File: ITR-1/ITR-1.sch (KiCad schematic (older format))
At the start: 50 parts, among them K1 Кнопка_KLS7-TS5401-1.35-250-T, K2 Кнопка_KLS7-TS5401-1.35-250-T, X1 отверстие_под_пайку, X2 отверстие_под_пайку

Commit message: аналоговые каналы перенесены на ADC1
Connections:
- net AN.2V5.REF: now also A1.8 (IO32/ADC1-4); no longer A1.12 (IO27/ADC2-7)
- net AN.BAT.MEASURE: now also A1.7 (IO35/ADC1-7); no longer A1.26 (IO4/ADC2-0)
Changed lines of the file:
@@
 Wire Wire Line
 	11000 3500 11675 3500
-Text Label 6750 10300 2    50   ~ 0
+Text Label 1750 9400 0    50   ~ 0
 AN.BAT.MEASURE
-Text Label 2000 10150 0    50   ~ 0
+Text Label 1750 9550 0    50   ~ 0
 AN.2V5.REF
 NoConn ~ 4650 10750
 NoConn ~ 2500 10300
 Wire Wire Line
-	6750 10300 5950 10300
+	1750 9400 2500 9400
 Wire Wire Line
 	5950 10000 6750 10000
@@
 $EndComp
 Wire Wire Line
-	2500 10150 2000 10150
+	2500 9550 1750 9550
 NoConn ~ 4800 10750
 $Comp

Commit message: изменено опорное + подключение к мотору; заготовка под 2 светодиода
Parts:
- added HL2: Светодиод_сдвоенный_KPB-3025SURKCGKC, N_VD_HL:Светодиод_SMD_m3025, symbol elements_2020:Светодиод_сдвоенный_KPB-3025SURKCGKC
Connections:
- net U.FB: now reaches DA1.1, R14.2, R15.1
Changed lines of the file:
@@
 Wire Wire Line
 	13000 1750 13000 4750
+Text Label 14500 5600 0    50   ~ 0
+U.FB
+$Comp
+L elements_2020:Светодиод_сдвоенный_KPB-3025SURKCGKC HL2
+U 1 1 6172B487
+P 8500 8800
+F 0 "HL2" H 8650 9031 60  0000 C CNN
+F 1 "Светодиод_сдвоенный_KPB-3025SURKCGKC" H 8650 9031 60  0001 C CNN
+F 2 "N_VD_HL:Светодиод_SMD_m3025" H 8800 8300 60  0001 C CNN
+F 3 "" H 8800 8300 60  0001 C CNN
+	1    8500 8800
+	1    0    0    -1
+$EndComp
 $EndSCHEMATC

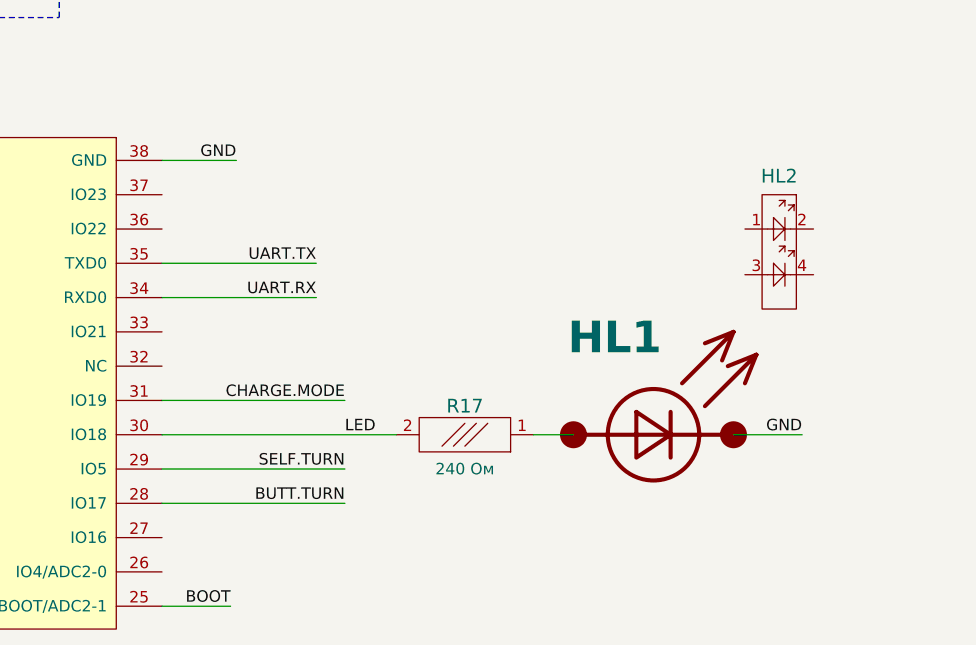
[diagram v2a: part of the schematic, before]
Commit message: модифицирована тайминги обмена с сервером, LED заменен на 2хцветный
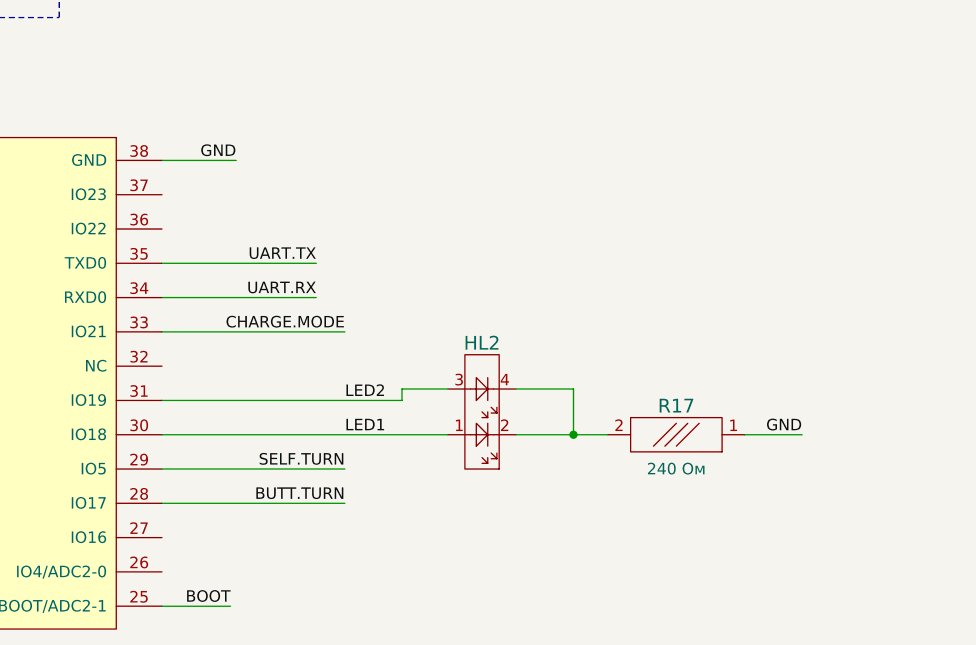
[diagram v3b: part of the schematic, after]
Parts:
- removed HL1: Светодиод, N_VD_HL:Светодиод_SMD_IEC_0603, symbol ITR-1-rescue:Светодиод-BIG_schemes
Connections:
- net CHARGE.MODE: now also A1.33 (IO21); no longer A1.31 (IO19)
- net GND: now also R17.1
- net LED1: now reaches HL2.1
- net LED1: now also A1.30 (IO18)
- net at HL2.2: now also HL2.4, R17.2
- net LED2: now reaches HL2.3
- net LED2: now also A1.31 (IO19)
- removed net LED: A1.30 (IO18), R17.2
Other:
- moved on the sheet: HL2, R17
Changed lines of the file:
@@
 Text Label 6275 8500 2    50   ~ 0
 GND
-Text Label 6750 9550 2    50   ~ 0
+Text Label 6750 9250 2    50   ~ 0
 CHARGE.MODE
 Text Label 6750 10000 2    50   ~ 0
@@
 	6625 8950 5950 8950
 Wire Wire Line
-	6750 9550 5950 9550
+	6750 9250 5950 9250
 Text Label 6250 10450 2    50   ~ 0
 BOOT
@@
 NoConn ~ 3600 10750
 Text Label 6750 9700 0    50   ~ 0
-LED
+LED1
 $Comp
 L elements:Клеммник_х3 XS2
@@
 L elements:Резистор_0,065Вт R17
 U 1 1 61468C4F
-P 7275 9700
-F 0 "R17" H 7275 9575 60  0000 C CNN
-F 1 "Резистор_0,065Вт" H 7275 9550 60  0001 C CNN
-F 2 "N_RLC:Резистор_SMD_0603_0,065_Вт" H 7275 9700 60  0001 C CNN
-F 3 "" H 7275 9700 60  0001 C CNN
-F 4 "R101" H 7275 9700 50  0001 C CNN "УГО"
-F 5 "240 Ом" H 7275 9850 50  0000 C CNN "INFO"
-	1    7275 9700
+P 8200 9700
+F 0 "R17" H 8200 9575 60  0000 C CNN
+F 1 "Резистор_0,065Вт" H 8200 9550 60  0001 C CNN
+F 2 "N_RLC:Резистор_SMD_0603_0,065_Вт" H 8200 9700 60  0001 C CNN
+F 3 "" H 8200 9700 60  0001 C CNN
+F 4 "R101" H 8200 9700 50  0001 C CNN "УГО"
+F 5 "240 Ом" H 8200 9850 50  0000 C CNN "INFO"
+	1    8200 9700
 	-1   0    0    1
 $EndComp
@@
 Wire Wire Line
 	5950 10000 6750 10000
-$Comp
-L ITR-1-rescue:Светодиод-BIG_schemes HL1
-U 1 1 61662DE6
-P 7750 9700
-F 0 "HL1" H 7725 10125 138 0000 L CNB
-F 1 "Светодиод" H 7850 9900 50  0001 C CNN
-F 2 "N_VD_HL:Светодиод_SMD_IEC_0603" H 8025 9700 50  0001 C CNN
-F 3 "" H 8025 9700 50  0001 C CNN
-F 4 "2.730" H 7850 10000 50  0001 C CNN "SYMBOL"
-	1    7750 9700
-	1    0    0    -1
-$EndComp
-Wire Wire Line
-	7575 9700 7750 9700
-Wire Wire Line
-	8450 9700 8750 9700
 Text Label 8750 9700 2    50   ~ 0
 GND
-Wire Wire Line
-	5950 9700 6975 9700
 Wire Wire Line
 	5950 9850 6750 9850
@@
 L elements_2020:Светодиод_сдвоенный_KPB-3025SURKCGKC HL2
 U 1 1 6172B487
-P 8500 8800
-F 0 "HL2" H 8650 9031 60  0000 C CNN
-F 1 "Светодиод_сдвоенный_KPB-3025SURKCGKC" H 8650 9031 60  0001 C CNN
-F 2 "N_VD_HL:Светодиод_SMD_m3025" H 8800 8300 60  0001 C CNN
-F 3 "" H 8800 8300 60  0001 C CNN
-	1    8500 8800
-	1    0    0    -1
-$EndComp
+P 7200 9700
+F 0 "HL2" H 7350 9300 60  0000 C CNN
+F 1 "Светодиод_сдвоенный_KPB-3025SURKCGKC" H 7350 9931 60  0001 C CNN
+F 2 "N_VD_HL:Светодиод_SMD_m3025" H 7500 9200 60  0001 C CNN
+F 3 "" H 7500 9200 60  0001 C CNN
+	1    7200 9700
+	1    0    0    1
+$EndComp
+Text Label 6750 9550 0    50   ~ 0
+LED2
+Wire Wire Line
+	5950 9700 7200 9700
+Wire Wire Line
+	5950 9550 7000 9550
+Wire Wire Line
+	7000 9550 7000 9500
+Wire Wire Line
+	7000 9500 7200 9500
+Wire Wire Line
+	7500 9700 7750 9700
+Wire Wire Line
+	7750 9500 7750 9700
+Wire Wire Line
+	7750 9500 7500 9500
+Wire Wire Line
+	7900 9700 7750 9700
+Connection ~ 7750 9700
+Wire Wire Line
+	8750 9700 8500 9700
 $EndSCHEMATC

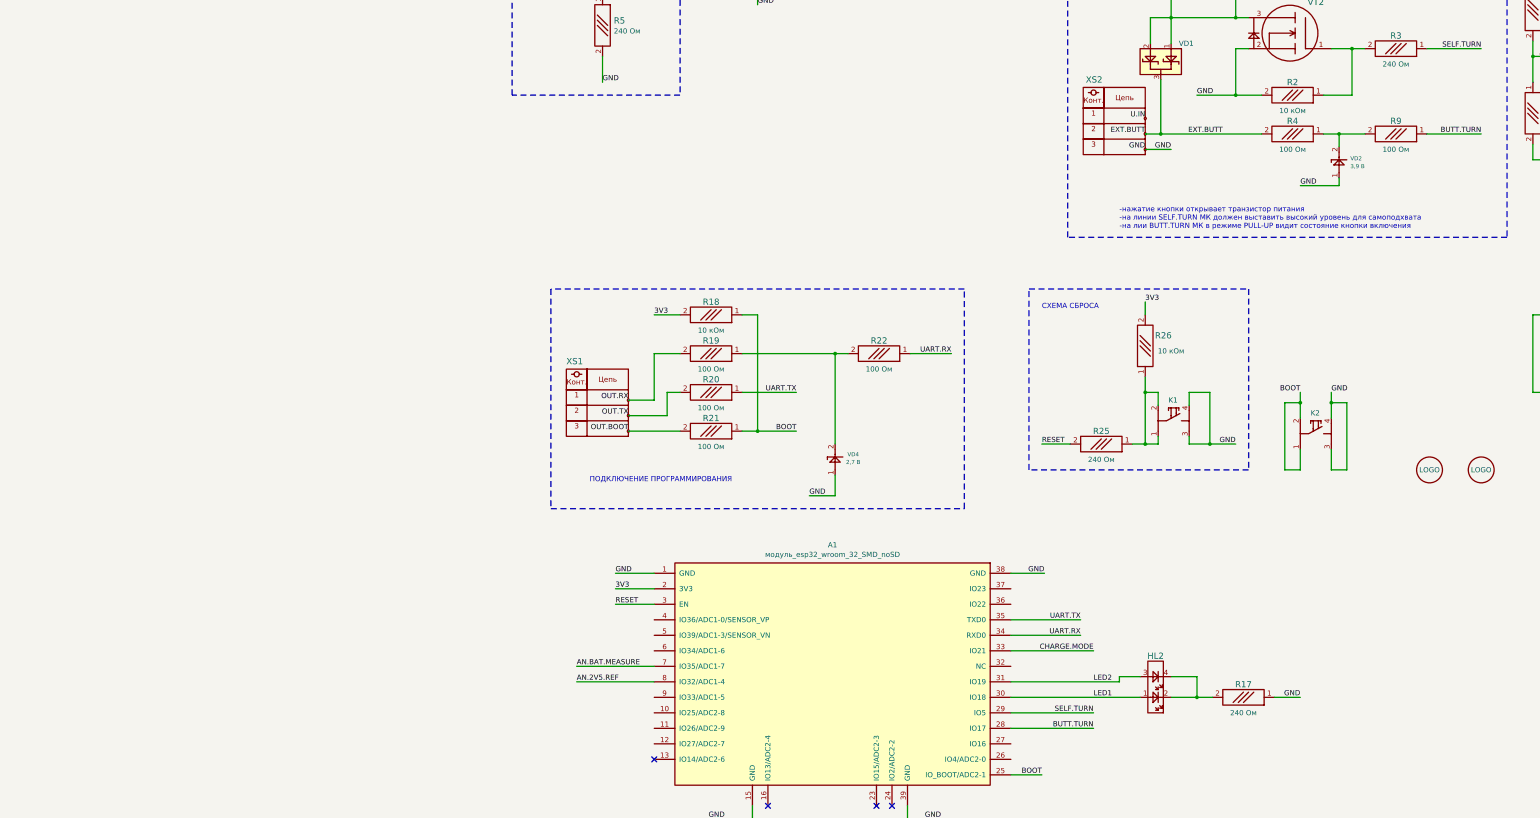
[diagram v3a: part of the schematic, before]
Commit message: зарядка через USB, в сервисный джек добавлена земля, кнопка впаивается
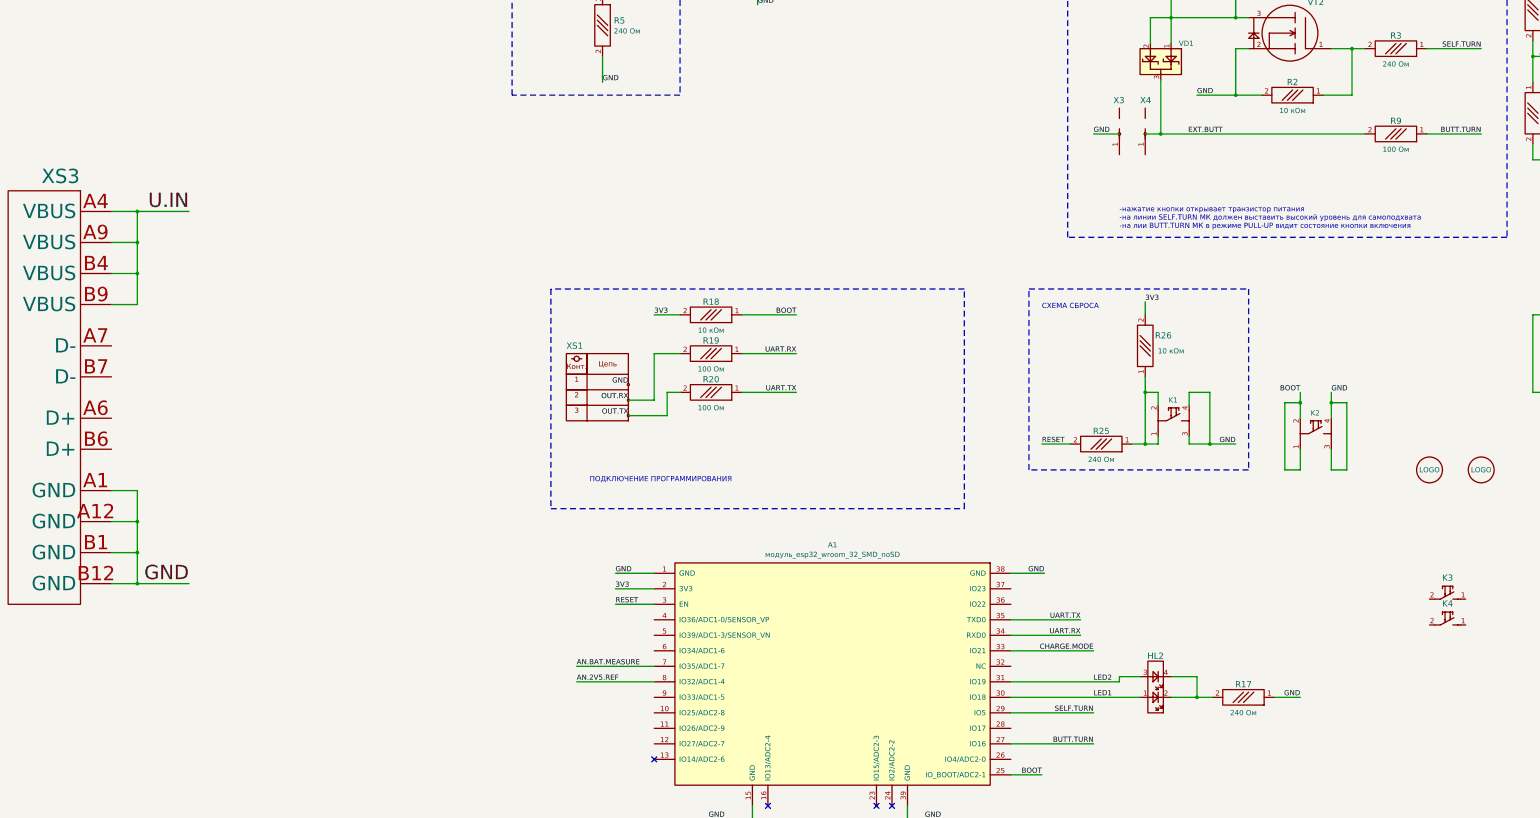
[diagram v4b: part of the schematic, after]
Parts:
- removed R21, R22, R4: Резистор_0,065Вт, N_RLC:Резистор_SMD_0603_0,065_Вт, symbol elements:Резистор_0,065Вт
- removed VD2: Стабилитрон_BZV55-C3V9, N_VD_HL:SOD-80, symbol elements_2020:Стабилитрон_1N5352BRLG_вертикальный
- removed VD4: Стабилитрон_BZV55C2V7, N_VD_HL:SOD-80, symbol elements_2020:Стабилитрон_1N5352BRLG_вертикальный
- removed XS2: Клеммник_х3, N_X:jack_ST-033, symbol elements:Клеммник_х3
- added K3, K4: кнопка, N_X:Кнопка_FSMSM, symbol elements:кнопка
- added X3, X4: отверстие_под_пайку, N_X:ОтверстиеD1.2, symbol elements:отверстие_под_пайку
- added XS3: UBS-type-C-105450-0101&упрощенная, N_X:usb-type-c, symbol elements_2020:UBS-type-C-105450-0101&упрощенная
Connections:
- net OUT.BOOT is gone; now on net OUT.TX: XS1.3
- net BUTT.TURN: now also A1.27 (IO16); no longer A1.28 (IO17)
- net EXT.BUTT: now also R9.2, X4.1
- net GND: now also XS1.1, X3.1, XS3.A1 (GND), XS3.A12 (GND), XS3.B1 (GND), XS3.B12 (GND)
- net OUT.RX: now also XS1.2; no longer XS1.1
- net OUT.TX: no longer XS1.2
- net U.IN: now also XS3.A4 (VBUS), XS3.A9 (VBUS), XS3.B4 (VBUS), XS3.B9 (VBUS)
- net UART.RX: now also R19.1
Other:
- moved on the sheet: XS1
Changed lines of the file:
@@
 EESchema Schematic File Version 4
-LIBS:ITR-1-cache
 EELAYER 30 0
 EELAYER END
@@
 ~~300 мА
 Wire Wire Line
-	7250 4400 7500 4400
+	7000 4250 6750 4250
 Wire Wire Line
 	8125 3875 7750 3875
@@
 Text Label 7750 3875 0    50   ~ 0
 GND
-Text Label 7500 4400 2    50   ~ 0
+Text Label 6750 4250 0    50   ~ 0
 GND
 Connection ~ 8125 3125
@@
 Wire Wire Line
 	10500 4250 9975 4250
-Wire Wire Line
-	9375 4250 9125 4250
 Connection ~ 7400 4250
 Text Notes 7000 5175 0    50   ~ 0
@@
 Text Label 6750 9250 2    50   ~ 0
 CHARGE.MODE
-Text Label 6750 10000 2    50   ~ 0
+Text Label 6750 10150 2    50   ~ 0
 BUTT.TURN
 Text Label 2125 8800 0    50   ~ 0
@@
 Text Label 6750 9700 0    50   ~ 0
 LED1
-$Comp
-L elements:Клеммник_х3 XS2
-U 1 1 6149F023
-P 7250 4100
-F 0 "XS2" H 6675 4475 60  0000 L CNN
-F 1 "Клеммник_х3" H 6950 3700 60  0001 C CNN
-F 2 "N_X:jack_ST-033" H 6675 4375 60  0001 C CNN
-F 3 "" H 6675 4375 60  0001 C CNN
-F 4 "https://www.chipdip.ru/product/st-033" H 7250 4100 50  0001 C CNN "LINK"
-	1    7250 4100
-	1    0    0    -1
-$EndComp
-Text Label 7250 4400 2    50   ~ 0
+Text Label -2000 8600 2    138  ~ 0
 GND
-Text Label 7250 4100 2    50   ~ 0
+Text Label -2000 5000 2    138  ~ 0
 U.IN
 Text Label 8000 4250 2    50   ~ 0
 EXT.BUTT
-Text Label 7250 4250 2    50   ~ 0
-EXT.BUTT
 Text Label 2250 6975 2    50   ~ 0
 OUT.TX
@@
 Wire Wire Line
 	2500 6375 2750 6375
-Text Label 4000 7750 0    50   ~ 0
-GND
-$Comp
-L elements:Резистор_0,065Вт R22
-U 1 1 61539EA6
-P 4675 6375
-F 0 "R22" H 4675 6250 60  0000 C CNN
-F 1 "Резистор_0,065Вт" H 4675 6225 60  0001 C CNN
-F 2 "N_RLC:Резистор_SMD_0603_0,065_Вт" H 4675 6375 60  0001 C CNN
-F 3 "" H 4675 6375 60  0001 C CNN
-F 4 "R101" H 4675 6375 50  0001 C CNN "УГО"
-F 5 "100 Ом" H 4675 6525 50  0000 C CNN "INFO"
-	1    4675 6375
-	-1   0    0    1
-$EndComp
-Text Label 5375 6375 2    50   ~ 0
+Text Label 3875 6375 2    50   ~ 0
 UART.RX
 Text Label 3875 6750 2    50   ~ 0
 UART.TX
 Wire Wire Line
-	4975 6375 5375 6375
+	3350 6375 3875 6375
 Text Notes 1875 7625 0    50   ~ 0
 ПОДКЛЮЧЕНИЕ ПРОГРАММИРОВАНИЯ
-Text Label 3875 7125 2    50   ~ 0
+Text Label 3875 6000 2    50   ~ 0
 BOOT
-$Comp
-L elements:Резистор_0,065Вт R21
-U 1 1 615C937D
-P 3050 7125
-F 0 "R21" H 3050 7000 60  0000 C CNN
-F 1 "Резистор_0,065Вт" H 3050 6975 60  0001 C CNN
-F 2 "N_RLC:Резистор_SMD_0603_0,065_Вт" H 3050 7125 60  0001 C CNN
-F 3 "" H 3050 7125 60  0001 C CNN
-F 4 "R101" H 3050 7125 50  0001 C CNN "УГО"
-F 5 "100 Ом" H 3050 7275 50  0000 C CNN "INFO"
-	1    3050 7125
-	-1   0    0    1
-$EndComp
-$Comp
-L elements_2020:Стабилитрон_1N5352BRLG_вертикальный VD4
-U 1 1 615D0D90
-P 4250 7550
-F 0 "VD4" V 4450 7375 39  0000 C CNN
-F 1 "Стабилитрон_BZV55C2V7" H 4425 7325 39  0001 C CNN
-F 2 "N_VD_HL:SOD-80" H 4400 7225 39  0001 C CNN
-F 3 "" H 4150 7550 39  0001 C CNN
-F 4 "2,7 В" V 4375 7375 39  0000 C CNN "INFO"
-F 5 "https://www.chipdip.ru/product/bzv55c2v7" H 4400 7125 50  0001 C CNN "LINK"
-	1    4250 7550
-	0    -1   -1   0
-$EndComp
-Wire Wire Line
-	4250 7750 4250 7550
-Wire Wire Line
-	3500 7125 3875 7125
-Text Label 2250 7125 2    50   ~ 0
-OUT.BOOT
-Wire Wire Line
-	2250 7125 2750 7125
 Wire Wire Line
 	2250 6975 2625 6975
@@
 Wire Wire Line
 	2500 6825 2500 6375
-Wire Wire Line
-	4250 6375 4375 6375
-Wire Wire Line
-	3350 6375 4250 6375
-Connection ~ 4250 6375
-Wire Wire Line
-	4250 7250 4250 6375
-Wire Wire Line
-	3350 7125 3500 7125
 $Comp
 L elements:Резистор_0,065Вт R18
@@
 	-1   0    0    1
 $EndComp
-Wire Wire Line
-	3350 6000 3500 6000
-Wire Wire Line
-	3500 6000 3500 7125
 Text Label 2500 6000 0    50   ~ 0
 3V3
@@
 L elements:Клеммник_х3 XS1
 U 1 1 617654B3
-P 2250 6825
-F 0 "XS1" H 1650 7200 60  0000 L CNN
-F 1 "Клеммник_х3" H 1950 6425 60  0001 C CNN
-F 2 "N_X:jack_ST-033" H 1675 7100 60  0001 C CNN
-F 3 "" H 1675 7100 60  0001 C CNN
-F 4 "https://www.chipdip.ru/product/st-033" H 2250 6825 50  0001 C CNN "LINK"
-	1    2250 6825
+P 2250 6675
+F 0 "XS1" H 1650 7050 60  0000 L CNN
+F 1 "Клеммник_х3" H 1950 6275 60  0001 C CNN
+F 2 "N_X:jack_ST-033" H 1675 6950 60  0001 C CNN
+F 3 "" H 1675 6950 60  0001 C CNN
+F 4 "https://www.chipdip.ru/product/st-033" H 2250 6675 50  0001 C CNN "LINK"
+	1    2250 6675
 	1    0    0    -1
 $EndComp
@@
 BAT.CHARGE
 Wire Wire Line
-	4000 7750 4250 7750
-Connection ~ 3500 7125
-Wire Wire Line
 	3350 6750 3875 6750
 $Comp
@@
 $EndComp
 $Comp
-L elements:Резистор_0,065Вт R4
-U 1 1 614A5C24
-P 8675 4250
-F 0 "R4" H 8675 4125 60  0000 C CNN
-F 1 "Резистор_0,065Вт" H 8675 4100 60  0001 C CNN
-F 2 "N_RLC:Резистор_SMD_0603_0,065_Вт" H 8675 4250 60  0001 C CNN
-F 3 "" H 8675 4250 60  0001 C CNN
-F 4 "R101" H 8675 4250 50  0001 C CNN "УГО"
-F 5 "100 Ом" H 8675 4400 50  0000 C CNN "INFO"
-	1    8675 4250
-	-1   0    0    1
-$EndComp
-$Comp
 L elements:Резистор_0,065Вт R9
 U 1 1 614A6645
@@
 	-1   0    0    1
 $EndComp
-Wire Wire Line
-	8375 4250 7400 4250
-Wire Wire Line
-	9125 4675 9125 4750
-Wire Wire Line
-	9125 4750 8750 4750
-Wire Wire Line
-	9125 4375 9125 4250
-Connection ~ 9125 4250
-Wire Wire Line
-	9125 4250 8975 4250
-Text Label 8750 4750 0    50   ~ 0
-GND
-$Comp
-L elements_2020:Стабилитрон_1N5352BRLG_вертикальный VD2
-U 1 1 614BD07A
-P 9125 4675
-F 0 "VD2" V 9313 4566 39  0000 R CNN
-F 1 "Стабилитрон_BZV55-C3V9" H 9300 4450 39  0001 C CNN
-F 2 "N_VD_HL:SOD-80" H 9275 4350 39  0001 C CNN
-F 3 "" H 9025 4675 39  0001 C CNN
-F 4 "3,9 В" V 9237 4566 39  0000 R CNN "INFO"
-F 5 "https://www.chipdip.ru/product/bzv55-c3v9.115" H 9275 4250 50  0001 C CNN "LINK"
-	1    9125 4675
-	0    -1   -1   0
-$EndComp
 $Comp
 L elements:Конденсатор_керамический C3
@@
 	1750 9400 2500 9400
 Wire Wire Line
-	5950 10000 6750 10000
+	5950 10150 6750 10150
 Text Label 8750 9700 2    50   ~ 0
 GND
@@
 Wire Wire Line
 	8750 9700 8500 9700
+$Comp
+L elements_2020:UBS-type-C-105450-0101&упрощенная XS3
+U 1 1 61A451AC
+P -2750 5000
+F 0 "XS3" H -2258 5339 138 0000 C CNN
+F 1 "UBS-type-C-105450-0101&упрощенная" H -2550 5700 50  0001 C CNN
+F 2 "N_X:usb-type-c" H -2750 5000 50  0001 C CNN
+F 3 "" H -2750 5000 50  0001 C CNN
+F 4 "https://www.chipdip.ru/product/105450-0101-molex" H -2750 5600 50  0001 C CNN "LINK"
+	1    -2750 5000
+	-1   0    0    -1
+$EndComp
+$Comp
+L elements:отверстие_под_пайку X4
+U 1 1 61A4A787
+P 7250 4250
+F 0 "X4" H 7200 4575 60  0000 L CNN
+F 1 "отверстие_под_пайку" H 7300 4220 60  0001 L CNN
+F 2 "N_X:ОтверстиеD1.2" H 7250 4250 60  0001 C CNN
+F 3 "" H 7250 4250 60  0001 C CNN
+	1    7250 4250
+	1    0    0    -1
+$EndComp
+$Comp
+L elements:отверстие_под_пайку X3
+U 1 1 61A4A791
+P 7000 4250
+F 0 "X3" H 6950 4575 60  0000 L CNN
+F 1 "отверстие_под_пайку" H 7050 4220 60  0001 L CNN
+F 2 "N_X:ОтверстиеD1.2" H 7000 4250 60  0001 C CNN
+F 3 "" H 7000 4250 60  0001 C CNN
+	1    7000 4250
+	-1   0    0    -1
+$EndComp
+Wire Wire Line
+	-2750 5000 -2500 5000
+Wire Wire Line
+	-2500 5000 -2500 5300
+Wire Wire Line
+	-2500 5900 -2750 5900
+Connection ~ -2500 5000
+Wire Wire Line
+	-2500 5000 -2000 5000
+Wire Wire Line
+	-2500 5600 -2750 5600
+Connection ~ -2500 5600
+Wire Wire Line
+	-2500 5600 -2500 5900
+Wire Wire Line
+	-2500 5300 -2750 5300
+Connection ~ -2500 5300
+Wire Wire Line
+	-2500 5300 -2500 5600
+Wire Wire Line
+	-2750 8600 -2500 8600
+Wire Wire Line
+	-2500 8600 -2500 8300
+Wire Wire Line
+	-2500 7700 -2750 7700
+Connection ~ -2500 8600
+Wire Wire Line
+	-2500 8600 -2000 8600
+Wire Wire Line
+	-2500 8000 -2750 8000
+Connection ~ -2500 8000
+Wire Wire Line
+	-2500 8000 -2500 7700
+Wire Wire Line
+	-2500 8300 -2750 8300
+Connection ~ -2500 8300
+Wire Wire Line
+	-2500 8300 -2500 8000
+$Comp
+L elements:кнопка K3
+U 1 1 61B34F09
+P 10350 8750
+F 0 "K3" H 10175 8956 60  0000 C CNN
+F 1 "кнопка" H 10175 8956 60  0001 C CNN
+F 2 "N_X:Кнопка_FSMSM" H 10225 8800 60  0001 C CNN
+F 3 "" H 10225 8800 60  0001 C CNN
+	1    10350 8750
+	1    0    0    -1
+$EndComp
+Wire Wire Line
+	7400 4250 9375 4250
+Text Label 2250 6675 2    50   ~ 0
+GND
+Wire Wire Line
+	3350 6000 3875 6000
+$Comp
+L elements:кнопка K4
+U 1 1 61C0E62A
+P 10350 9000
+F 0 "K4" H 10175 9206 60  0000 C CNN
+F 1 "кнопка" H 10175 9206 60  0001 C CNN
+F 2 "N_X:Кнопка_FSMSM" H 10225 9050 60  0001 C CNN
+F 3 "" H 10225 9050 60  0001 C CNN
+	1    10350 9000
+	1    0    0    -1
+$EndComp
 $EndSCHEMATC
